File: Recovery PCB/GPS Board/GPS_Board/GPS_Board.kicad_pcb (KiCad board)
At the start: 2 copper layers, 85.7 x 50.8 mm, 9 parts, among them J1 XT30-M, J2 XT30-M, U1 Teensy4.1, U2 D24V22F5_VoltageRegulator, U3 LD1117v33

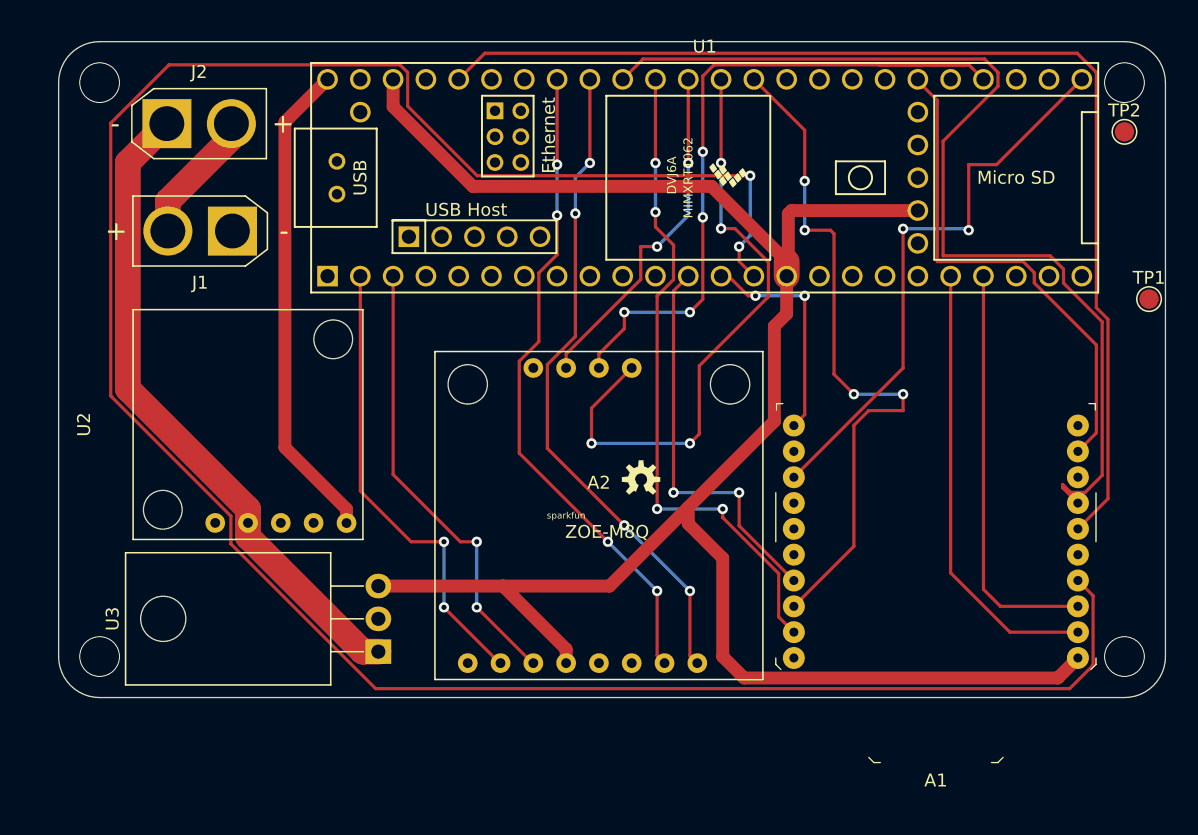
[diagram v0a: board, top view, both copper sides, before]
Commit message: Fixed power routing
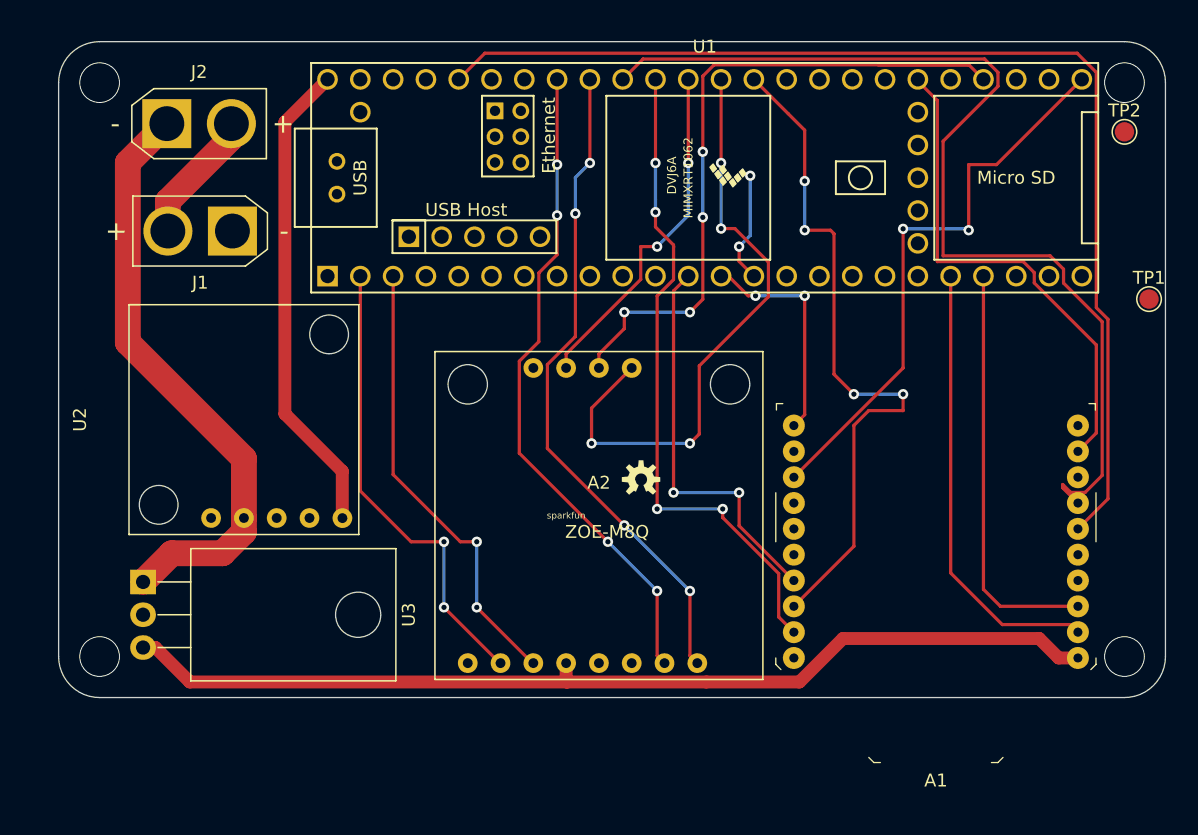
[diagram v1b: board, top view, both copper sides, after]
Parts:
- moved U3 19.0 mm to (117.7, 102.2), turned to 270 degrees
- moved U2 0.50 mm to (125.5, 89.6)
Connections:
- U1 pad 15: +3V3 -> Net-(U1-Pad15)
- U1 pad 46: +3V3 -> Net-(U1-Pad46)
- U1 pad 51: +3V3 -> Net-(U1-Pad51)
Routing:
- net /XBee_MISO: track 180.8 -> 8.61 mm
- net +3V3: track 149.7 -> 77.0 mm
- net Net-(J2-Pad1): track 50.9 -> 46.0 mm

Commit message: Routed data traces from GPS
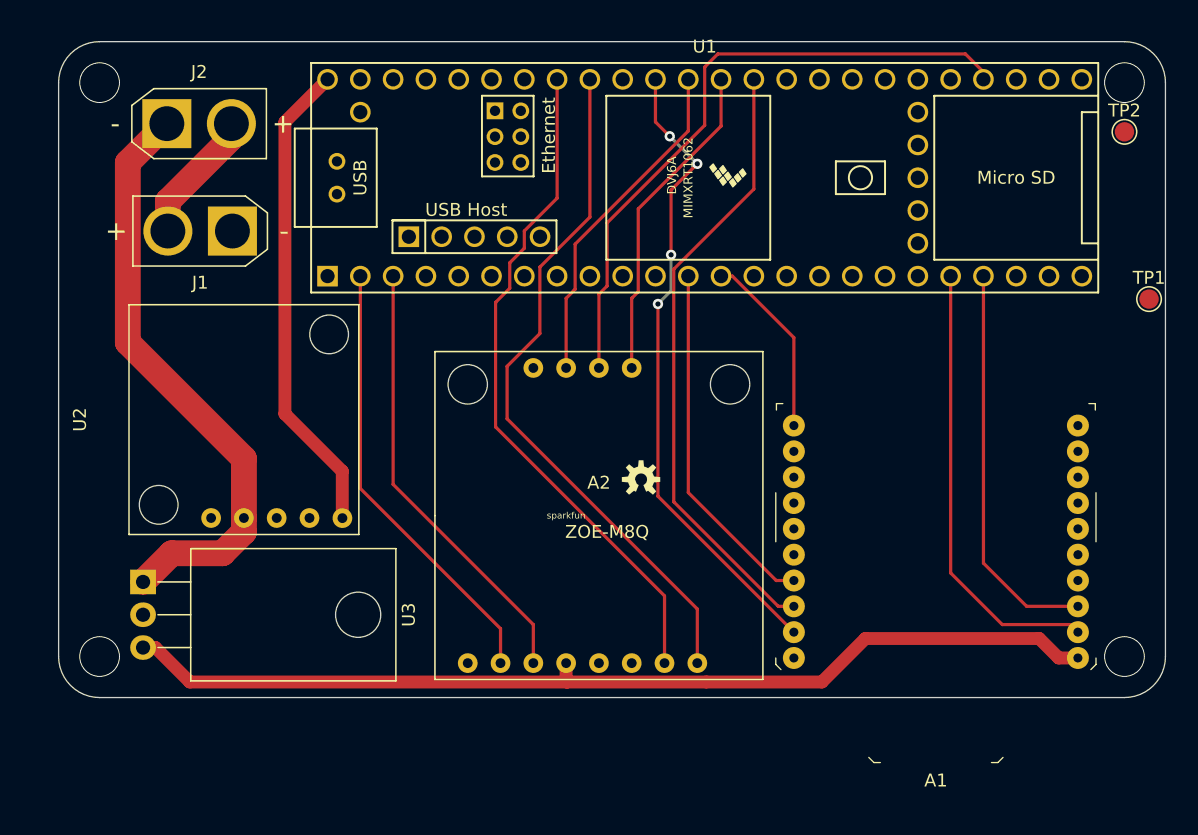
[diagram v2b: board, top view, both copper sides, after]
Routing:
- net /XBee_PWM: track 87.5 -> 0.00 mm
- net /XBEE_SDA: track 78.9 -> 0.00 mm
- net /XBEE_SLEEP: track 44.4 -> 0.00 mm, vias 2 -> 0
- net /XBee_DTR: track 39.0 -> 0.00 mm
- net /GPS_INT: track 47.6 -> 25.8 mm, vias 4 -> 0
- net /GPS_RESET: track 58.6 -> 49.9 mm, vias 4 -> 0
- net /XBee_MISO: track 8.61 -> 0.00 mm, vias 2 -> 0
- net /XBee_SCK: track 54.1 -> 47.9 mm, vias 4 -> 0
- net /XBee_CS: track 30.9 -> 27.8 mm, vias 2 -> 0
- net /XBee_MOSI: track 17.5 -> 14.4 mm, vias 2 -> 0
- net /GPS_SDA: track 51.4 -> 54.0 mm, vias 4 -> 0
- net /XBEE_SCL: track 51.5 -> 50.0 mm
- net /GPS_TX: track 36.0 -> 34.5 mm, vias 2 -> 0
- net /GPS_SCL: track 51.1 -> 52.6 mm, vias 4 -> 0
- net /XBEE_RX: track 32.1 -> 30.9 mm
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
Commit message: Routed all traces and removed vias
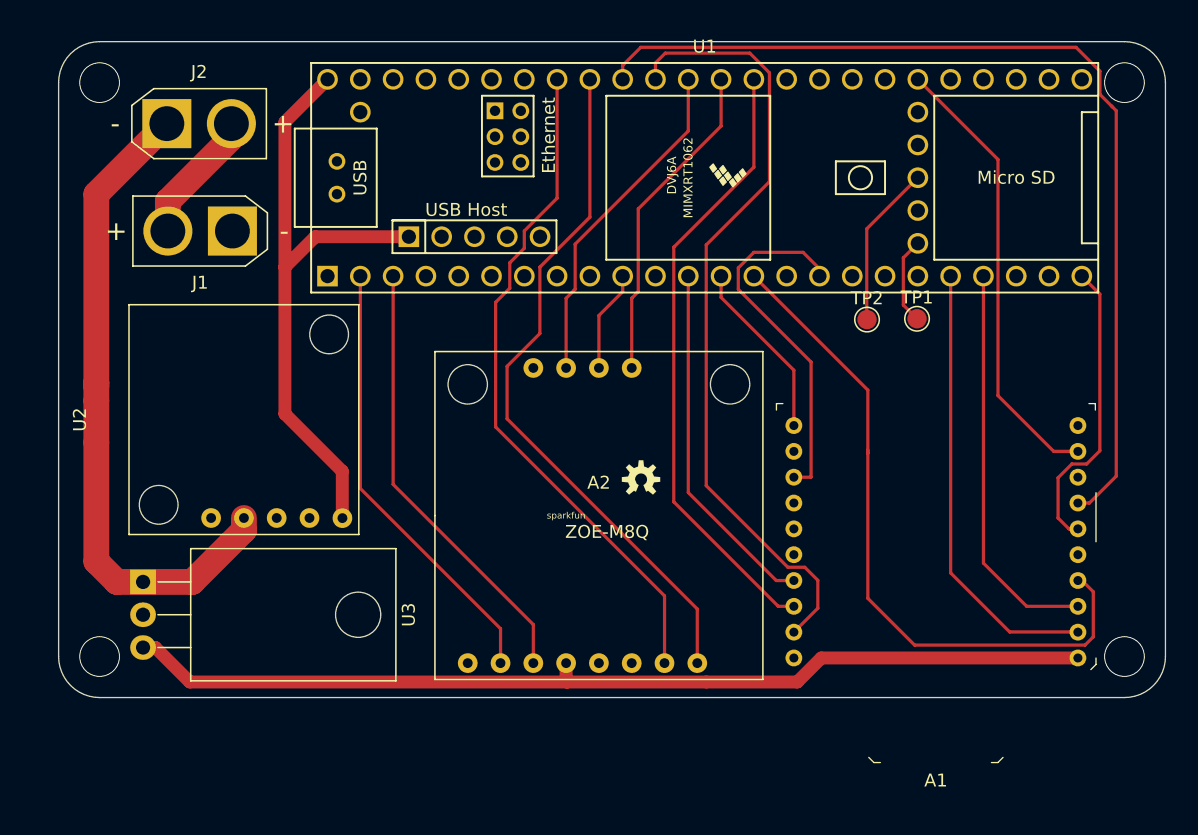
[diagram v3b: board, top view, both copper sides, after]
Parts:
- moved TP2 24.7 mm to (173.7, 81.9)
- moved TP1 18.0 mm to (177.6, 81.8)
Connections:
- U1 pad 10: Net-(U1-Pad10) -> /GPS_RESET
- U1 pad 16: Net-(U1-Pad16) -> /XBEE_SLEEP
- U1 pad 24: Net-(U1-Pad24) -> /XBee_PWM
- U1 pad 25: /XBEE_SLEEP -> Net-(U1-Pad25)
- U1 pad 28: /GPS_RESET -> Net-(U1-Pad28)
- U1 pad 44: /XBee_PWM -> Net-(U1-Pad44)
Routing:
- net /XBEE_SDA: track 0.00 -> 75.3 mm
- net /XBee_MISO: track 0.00 -> 53.1 mm
- net /GPS_RESET: track 49.9 -> 7.94 mm
- net /XBee_DTR: track 0.00 -> 35.0 mm
- net /XBEE_SLEEP: track 0.00 -> 27.8 mm
- net /XBee_PWM: track 0.00 -> 23.2 mm
- net GND: track 0.00 -> 12.5 mm
- net /XBEE_SCL: track 50.0 -> 61.7 mm, vias 4 -> 0
- net +5V: track 37.2 -> 47.8 mm
- net Net-(TP1-Pad1): track 0.00 -> 6.75 mm
- net Net-(J2-Pad1): track 46.0 -> 51.2 mm
- net +3V3: track 77.0 -> 75.8 mm
- net /XBee_MOSI: track 14.4 -> 13.9 mm

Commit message: Added test points
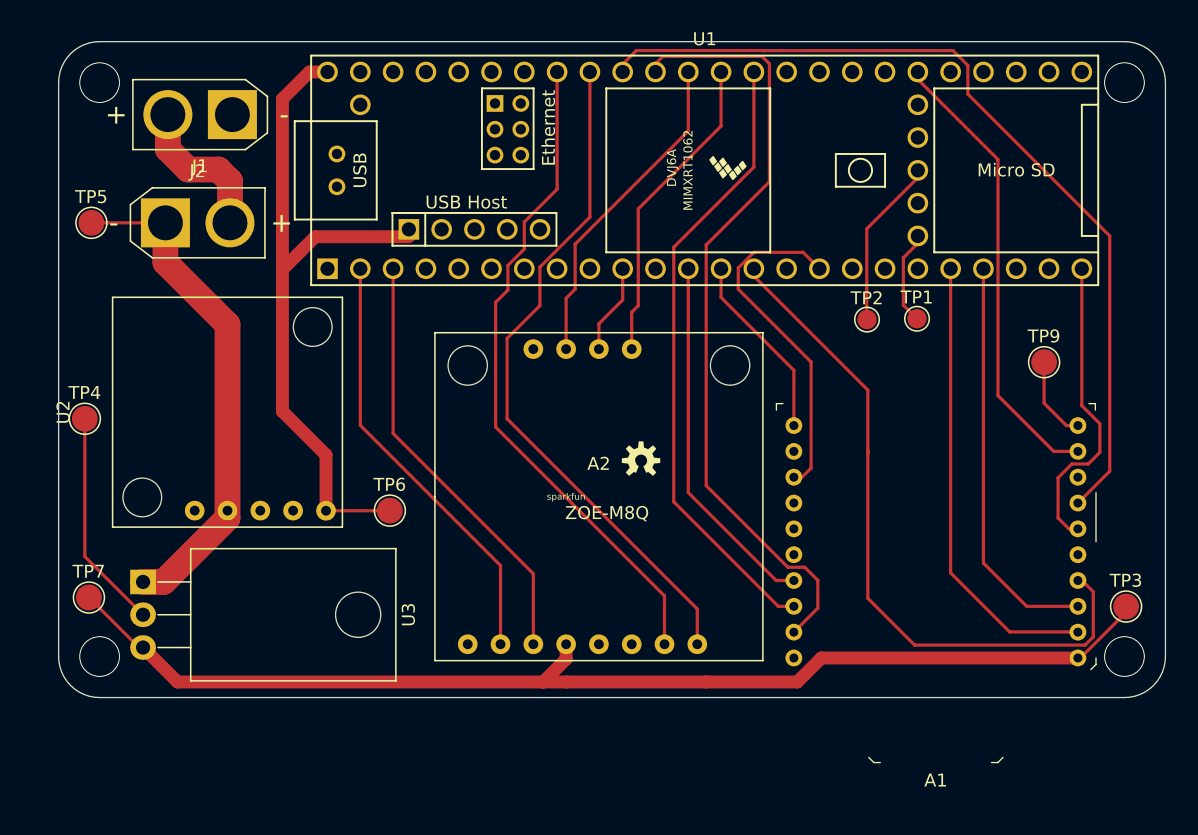
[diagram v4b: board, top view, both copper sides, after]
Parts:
- added TP3: TestPoint, TestPoint:TestPoint_Pad_D2.0mm, F.Cu at (193.8, 104.1)
- added TP4: TestPoint, TestPoint:TestPoint_Pad_D2.0mm, F.Cu at (113.2, 89.5)
- added TP5: TestPoint, TestPoint:TestPoint_Pad_D2.0mm, F.Cu at (113.7, 74.4)
- added TP6: TestPoint, TestPoint:TestPoint_Pad_D2.0mm, F.Cu at (136.8, 96.6)
- added TP7: TestPoint, TestPoint:TestPoint_Pad_D2.0mm, F.Cu at (113.5, 103.4)
- added TP9: TestPoint, TestPoint:TestPoint_Pad_D2.0mm, F.Cu at (187.5, 85.2)
- moved J1 9.02 mm to (124.6, 66.0)
- moved J2 7.68 mm to (119.4, 74.4)
- moved A2 1.46 mm to (153.0, 95.6)
- moved U2 1.39 mm to (124.2, 89.0)
- moved U1 0.57 mm to (161.2, 70.3)
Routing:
- net GND: track 12.5 -> 36.1 mm
- net +3V3: track 75.8 -> 88.6 mm
- net Net-(J2-Pad1): track 51.2 -> 39.2 mm
- net /XBEE_SDA: track 75.3 -> 68.3 mm
- net +5V: track 47.8 -> 53.4 mm
- net /GPS_INT: track 25.8 -> 23.8 mm
- net /GPS_RESET: track 7.94 -> 6.41 mm
- net /GPS_TX: track 34.5 -> 33.0 mm
- net /GPS_SDA: track 54.0 -> 52.5 mm
- net /GPS_SCL: track 52.6 -> 51.1 mm
- net /GPS_RX: track 34.5 -> 33.0 mm
- net /GPS_PPS: track 26.3 -> 24.8 mm
- net Net-(J1-Pad2): track 10.4 -> 11.8 mm

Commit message: Added pad for heat dissipation
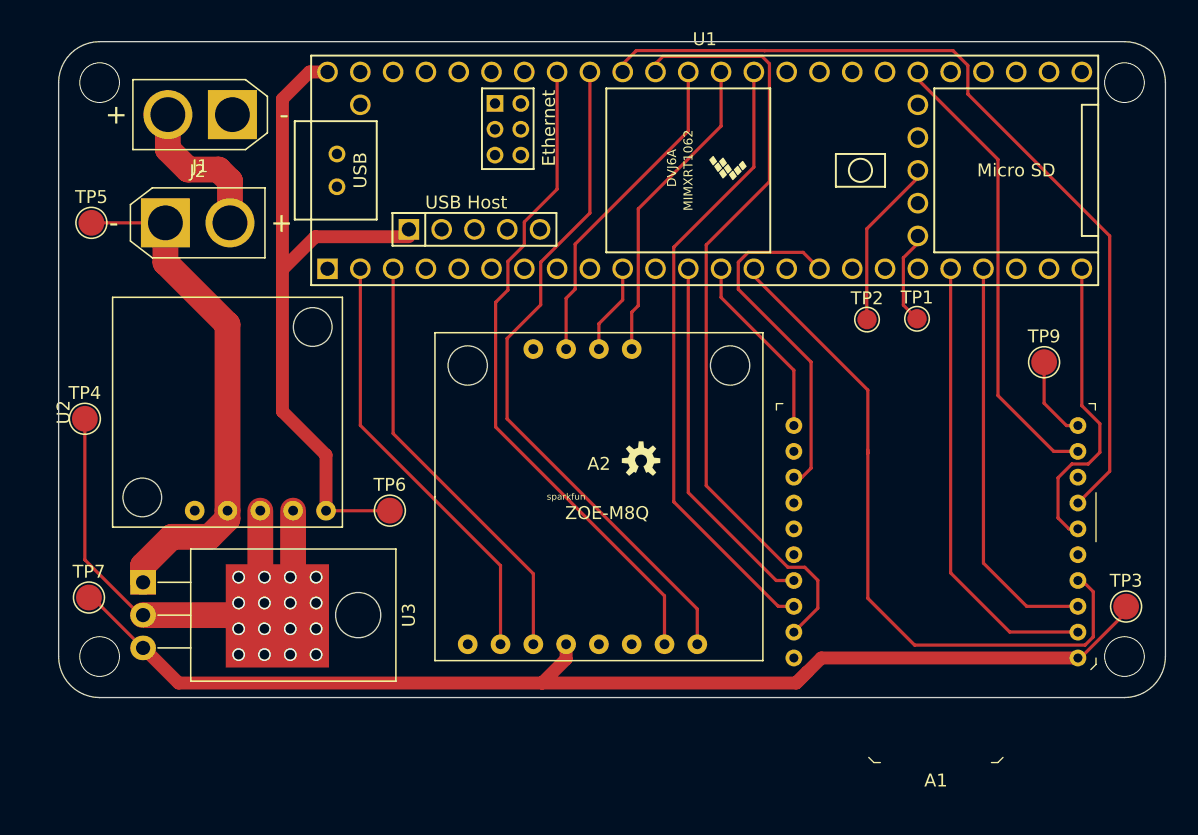
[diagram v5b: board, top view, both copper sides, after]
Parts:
- moved U3 10.7 mm to (128.1, 104.8)
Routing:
- net GND: track 36.1 -> 64.0 mm, vias 0 -> 16
- net +3V3: track 88.6 -> 89.8 mm
- net Net-(J2-Pad1): track 39.2 -> 40.0 mm

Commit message: Added connectors and updated traces.
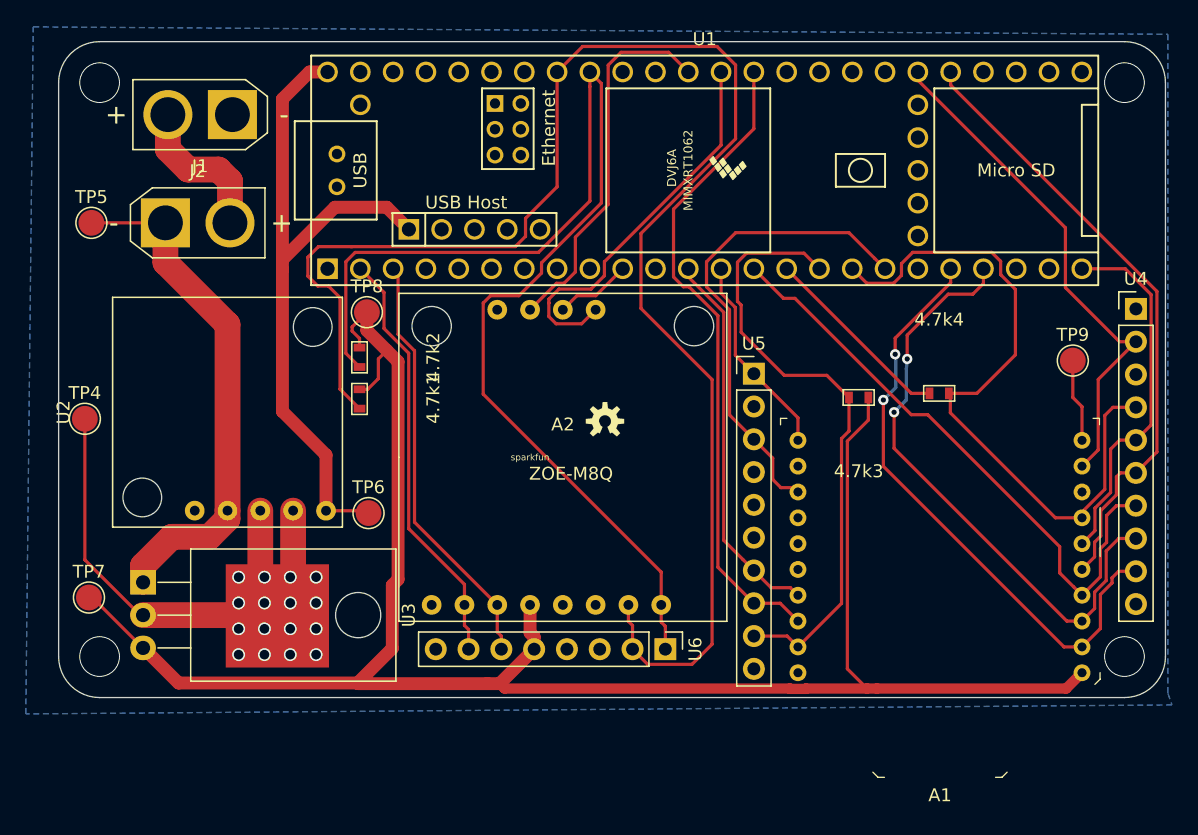
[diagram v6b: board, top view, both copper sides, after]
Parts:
- removed TP1, TP2: TestPoint, TestPoint:TestPoint_Pad_D1.5mm
- removed TP3: TestPoint, TestPoint:TestPoint_Pad_D2.0mm
- added 4.7k1: R_Small_US, GPS Board:0603, F.Cu at (134.4, 88.0)
- added 4.7k2: R_Small_US, GPS Board:0603, F.Cu at (134.4, 84.8)
- added 4.7k3: R_Small_US, GPS Board:0603, F.Cu at (173.1, 87.9)
- added 4.7k4: R_Small_US, GPS Board:0603, F.Cu at (179.3, 87.6)
- added TP8: TestPoint, TestPoint:TestPoint_Pad_D2.0mm, F.Cu at (135.0, 81.3)
- added U4: conn_recovery10, Connector_PinHeader_2.54mm:PinHeader_1x10_P2.54mm_Vertical, F.Cu at (194.6, 81.0)
- added U5: conn_recovery10, Connector_PinHeader_2.54mm:PinHeader_1x10_P2.54mm_Vertical, F.Cu at (165.0, 86.0)
- added U6: conn_recovery8, Connector_PinHeader_2.54mm:PinHeader_1x08_P2.54mm_Vertical, F.Cu at (158.1, 107.4)
- moved A2 4.13 mm to (150.2, 92.5)
- moved TP9 2.23 mm to (189.7, 85.0)
- moved TP6 1.66 mm to (135.1, 96.8)
- moved A1 1.19 mm to (179.4, 100.2)
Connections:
- net /XBee_CS renamed /XBEE_CS
- net /XBee_DTR renamed /XBEE_DTR
- net /XBee_MISO renamed /XBEE_MISO
- net /XBee_MOSI renamed /XBEE_MOSI
- net /XBee_PWM renamed /XBEE_PWM
- net /XBee_SCK renamed /XBEE_SCK
- A1 pad 5: /XBee_Reset -> /XBEE_RESET
- U1 pad 15: Net-(U1-Pad15) -> +3V3
- U1 pad 16: /XBEE_SLEEP -> /XBEE_SCL
- U1 pad 17: Net-(U1-Pad17) -> /XBEE_SDA
- U1 pad 18: Net-(U1-Pad18) -> /XBEE_SLEEP
- U1 pad 29: /XBee_RESET -> /XBEE_RESET
- U1 pad 38: /XBEE_SCL -> Net-(U1-Pad38)
- U1 pad 39: /XBEE_SDA -> Net-(U1-Pad39)
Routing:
- net +3V3: track 89.8 -> 165.4 mm
- net /GPS_SCL: track 51.1 -> 121.5 mm
- net /XBEE_RESET: track 0.00 -> 48.3 mm
- net /GPS_SDA: track 52.5 -> 95.4 mm
- net /XBEE_RX: track 30.9 -> 46.9 mm, vias 0 -> 2
- net /XBEE_SDA: track 68.3 -> 54.3 mm
- net /XBEE_SCL: track 61.9 -> 48.4 mm
- net GND: track 64.0 -> 51.4 mm
- net /XBEE_TX: track 34.7 -> 47.0 mm, vias 0 -> 2
- net /XBEE_SLEEP: track 27.6 -> 37.3 mm
- net Net-(U1-Pad50): track 6.75 -> 0.00 mm
- net /XBEE_MISO: track 53.1 -> 46.6 mm
- net /GPS_INT: track 23.8 -> 30.2 mm
- net /XBEE_PWM: track 23.3 -> 28.4 mm
- net /XBEE_DTR: track 35.0 -> 40.0 mm
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- added copper zone on B.Cu, net GND

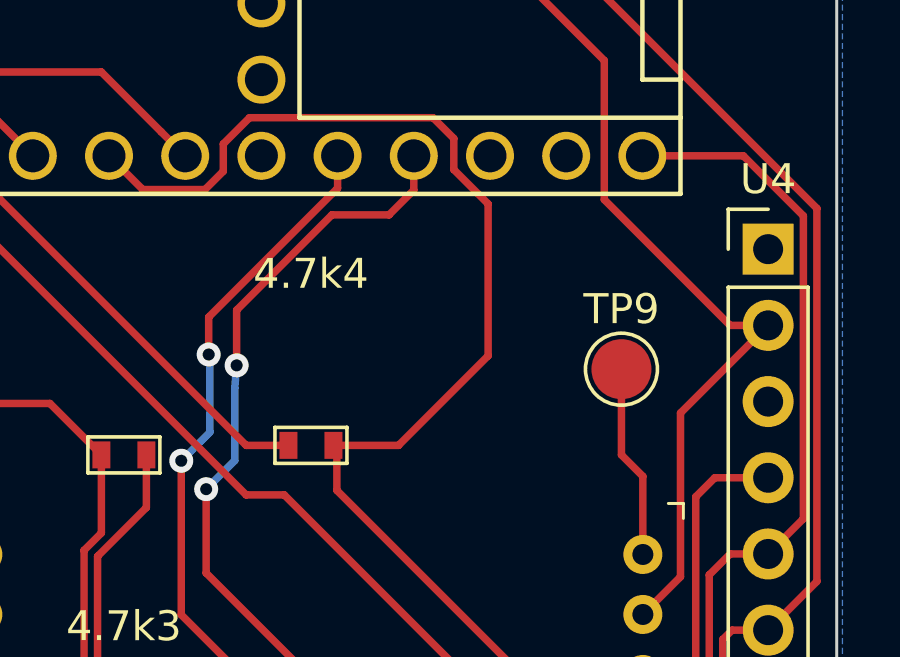
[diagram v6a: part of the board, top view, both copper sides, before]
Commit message: Added payload logo
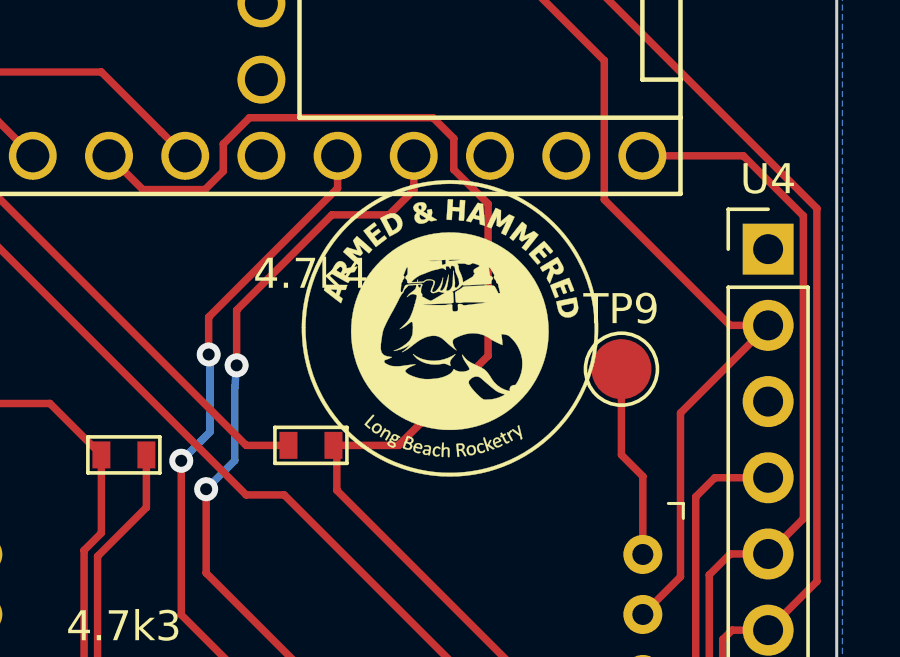
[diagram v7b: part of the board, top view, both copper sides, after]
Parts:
- added G***: LOGO, GPS Board:PayloadLogo, F.Cu at (184.0, 83.7)
